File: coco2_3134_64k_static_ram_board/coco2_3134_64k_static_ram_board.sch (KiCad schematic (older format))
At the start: 9 parts, among them CN3 Conn_01x12_Male, CN4 Conn_01x12_Male, J1 Conn_01x04_Female, U1 SN74HCT573PWR, U2 IS61C5128AS-25TLI, U3 SN74HCT32DR

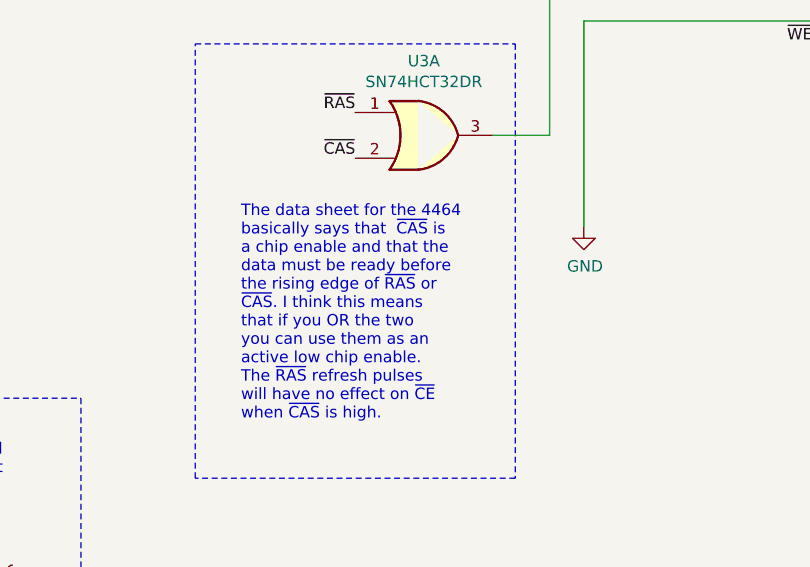
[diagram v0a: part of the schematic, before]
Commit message: added images and BOM
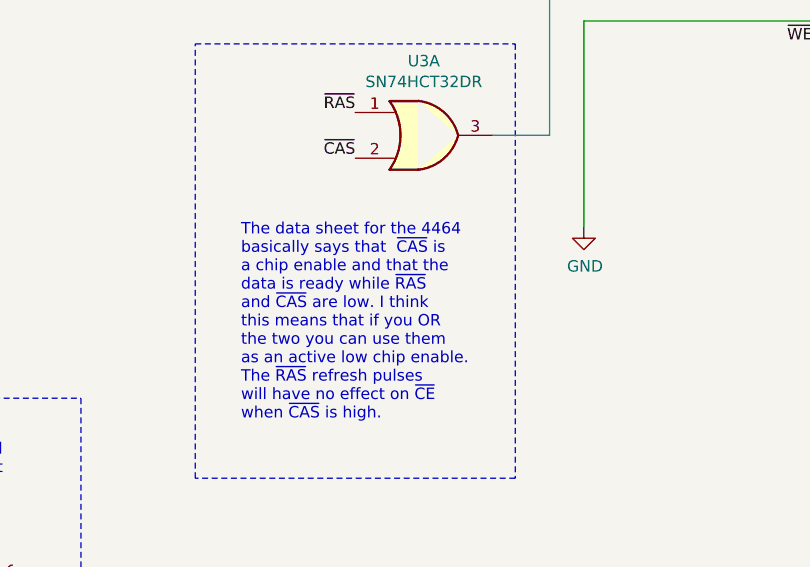
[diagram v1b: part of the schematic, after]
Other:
- note added: "The data sheet for the 4464\nbasically says that ~CAS~ is\na chip enable and that the\ndata is ready while ~RAS~\nand ~CAS~ are low. I think\nthis means that if you OR\nthe two you can use them\nas an active low chip enable.\nThe ~RAS~ refresh pulses\nwill have no effect on ~CE~\nwhen ~CAS~ is high."
- note removed: "The data sheet for the 4464\nbasically says that ~CAS~ is\na chip enable and that the\ndata must be ready before\nthe rising edge of ~RAS~ or\n~CAS~. I think this means \nthat if you OR the two\nyou can use them as an\nactive low chip enable.\nThe ~RAS~ refresh pulses\nwill have no effect on ~CE~\nwhen ~CAS~ is high."
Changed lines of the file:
@@
 	3550 7200 3550 7450
 Text Notes 5750 5900 0    50   ~ 0
-The data sheet for the 4464\nbasically says that  ~CAS~ is\na chip enable and that the\ndata must be ready before\nthe rising edge of ~RAS~ or\n~CAS~. I think this means \nthat if you OR the two\nyou can use them as an\nactive low chip enable.\nThe ~RAS~ refresh pulses\nwill have no effect on ~CE~\nwhen ~CAS~ is high.
+The data sheet for the 4464\nbasically says that  ~CAS~ is\na chip enable and that the\ndata is ready while ~RAS~\nand ~CAS~ are low. I think\nthis means that if you OR\nthe two you can use them\nas an active low chip enable.\nThe ~RAS~ refresh pulses\nwill have no effect on ~CE~\nwhen ~CAS~ is high.
 Text Notes 4500 1450 0    50   ~ 0
 This design is inspired by several projects.\nhttps://github.com/jamarju/c64-sram\nwhich in turn was inspired by\nhttps://postlmg.cc/Ty3Ff6sb\nAnd also Ciaran Ascomb's 512k\nSRAM board for the CoCo 3.\nhttps://gitlab.com/sixxie/cc3-512k

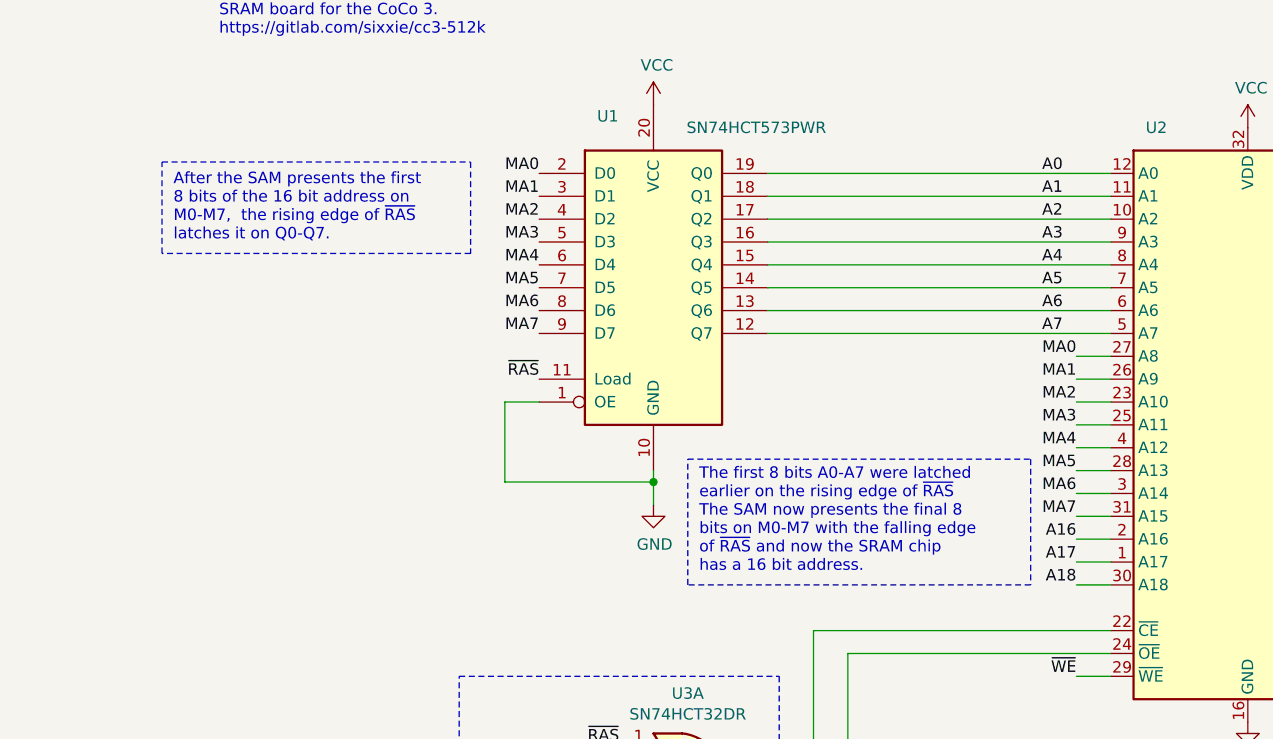
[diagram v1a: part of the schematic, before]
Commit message: made corrections to descriptions on how the address is converted for use with the SRAM chip
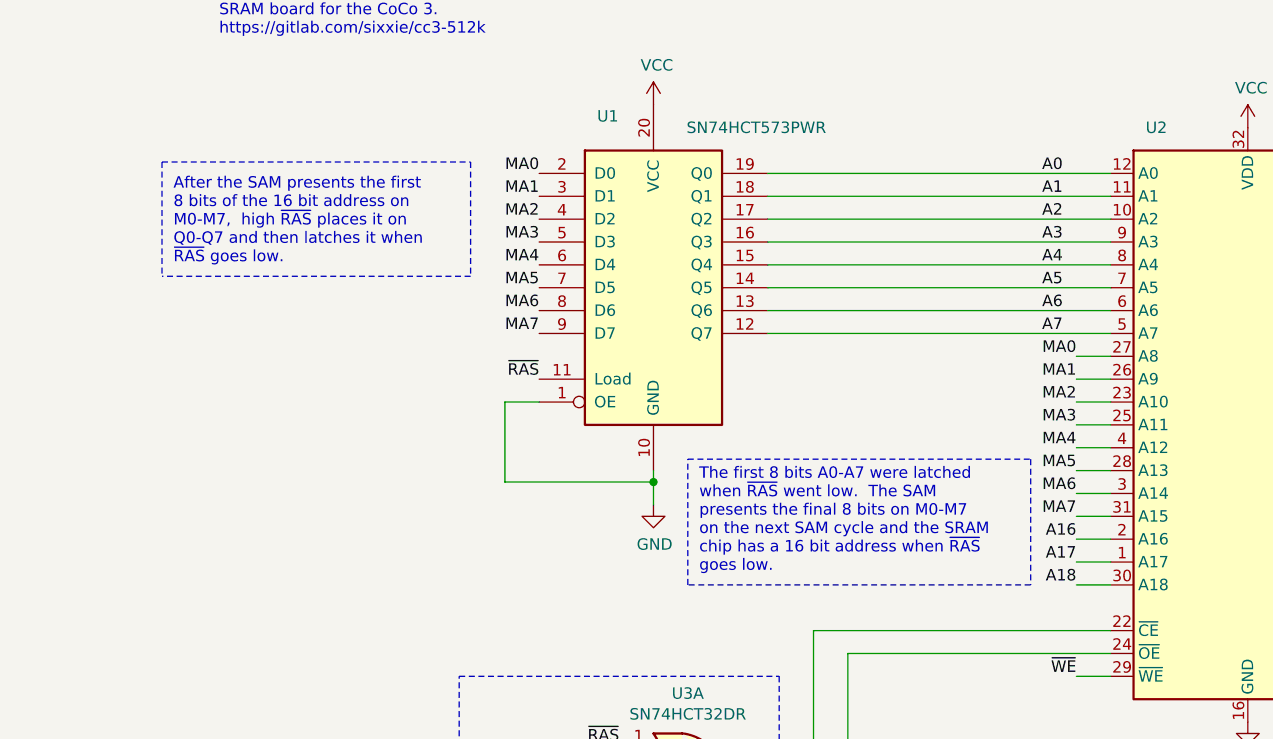
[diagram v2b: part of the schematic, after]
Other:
- note added: "After the SAM presents the first\n8 bits of the 16 bit address on\nM0-M7, high ~RAS~ places it on\nQ0-Q7 and then latches it when \n~RAS~ goes low."
- note added: "The first 8 bits A0-A7 were latched\nwhen ~RAS~ went low. The SAM\npresents the final 8 bits on M0-M7\non the next SAM cycle and the SRAM\nchip has a 16 bit address when ~RAS~\ngoes low.\n"
- note removed: "After the SAM presents the first\n8 bits of the 16 bit address on\nM0-M7, the rising edge of ~RAS~\nlatches it on Q0-Q7."
- note removed: "The first 8 bits A0-A7 were latched\nearlier on the rising edge of ~RAS~ \nThe SAM now presents the final 8\nbits on M0-M7 with the falling edge\nof ~RAS~ and now the SRAM chip\nhas a 16 bit address.\n"
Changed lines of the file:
@@
 Wire Notes Line
 	6950 4250 6950 6150
-Text Notes 4300 2350 0    50   ~ 0
-After the SAM presents the first\n8 bits of the 16 bit address on\nM0-M7,  the rising edge of ~RAS~\nlatches it on Q0-Q7.
+Text Notes 4300 2450 0    50   ~ 0
+After the SAM presents the first\n8 bits of the 16 bit address on\nM0-M7,  high ~RAS~ places it on\nQ0-Q7 and then latches it when \n~RAS~ goes low.
 Text Notes 6600 3800 0    50   ~ 0
-The first 8 bits A0-A7 were latched\nearlier on the rising edge of ~RAS~ \nThe SAM now presents the final 8\nbits on M0-M7 with the falling edge\nof ~RAS~ and now the SRAM chip\nhas a 16 bit address.\n
+The first 8 bits A0-A7 were latched\nwhen ~RAS~ went low.  The SAM\npresents the final 8 bits on M0-M7\non the next SAM cycle and the SRAM\nchip has a 16 bit address when ~RAS~\ngoes low.\n
 Wire Wire Line
 	6900 2050 8400 2050
@@
 	4250 2000 5600 2000
 Wire Notes Line
-	5600 2000 5600 2400
-Wire Notes Line
-	5600 2400 4250 2400
-Wire Notes Line
-	4250 2400 4250 2000
+	5600 2500 4250 2500
 Text Notes 3600 6300 0    50   ~ 0
 A16-A18 are the extra address\nlines on this chip that are pulled\nlow but also on a header so that\npeople can use it for bank\nswitching or whatever.
@@
 Wire Notes Line
 	3200 7750 3200 5800
+Wire Notes Line
+	5600 2000 5600 2500
+Wire Notes Line
+	4250 2000 4250 2500
 $EndSCHEMATC
